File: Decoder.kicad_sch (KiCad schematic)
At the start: 4 parts, among them U1 74LS04, U12 74LS00, U14 74LS138, U7 74LS32

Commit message: Schematic in progress
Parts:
- removed U14: 74LS138, DIP-16__300, symbol 74xx:74LS138
- added U58: 74LS688, symbol 74xx:74LS688
- added U59: 74LS138, Package_DIP:DIP-16_W7.62mm_Socket_LongPads, symbol 74xx:74LS138
- U1, U7: footprint DIP-14__300 -> Package_DIP:DIP-14_W7.62mm_Socket_LongPads
- U21: renamed from U12; footprint DIP-14__300 -> Package_DIP:DIP-14_W7.62mm_Socket_LongPads
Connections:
- net /VMA: now also U58.1 (G)
- net GND: now also U58.10 (GND), U59.16 (VCC)
- net SHADOW-IO: now also U58.2 (P0)
- net VCC: now also U58.12 (R4), U58.14 (R5), U58.16 (R6), U58.17 (P7), U58.18 (R7), U58.20 (VCC), U58.3 (R0), U58.4 (P1), U58.5 (R1), U58.7 (R2), U58.9 (R3), U59.6 (E3), U59.8 (GND)
- net mA10: now also U58.8 (P3)
- net mA11: now also U58.6 (P2)
- net mA8: now also U58.13 (P5)
- net mA9: now also U58.11 (P4)
- new net: U58.19 (P=R), U59.4 (E1), U59.5 (E2)
- new net mA4: U59.1 (A0)
- new net mA5: U59.2 (A1)
- new net mA6: U59.3 (A2)
- new net mA7: U58.15 (P6)
- new net /IOSEL-0EF80: U59.15 (O0)
- new net /IOSEL-0EF90: U59.14 (O1)
- new net /IOSEL-0EFA0: U59.13 (O2)
- new net /IOSEL-0EFB0: U59.12 (O3)
- new net /IOSEL-0EFC0: U59.11 (O4)
- new net /IOSEL-0EFD0: U59.10 (O5)
- new net /IOSEL-0EFE0: U59.9 (O6)
- new net /IOSEL-0EFF0: U59.7 (O7)
- no-connect marks 2 -> 0
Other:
- note added: "$E800 - $E8FF available $E900 - $E9FF available $EA00 - $EAFF MMU CONTROL (20?) $EB00 - $EBFF Video (3) $EC00 - $ECFF VIA0 (16) $ED00 - $EDFF VIA1 (16) $EE00 - $EEFF RTC (16) $EF00 - $EFFF ACIA (4)"
- note removed: "$E800 - $E8FF PTM $E900 - $E9FF available $EA00 - $EAFF MMU CONTROL $EB00 - $EBFF available $EC00 - $ECFF VIA0 $ED00 - $EDFF VIA1 $EE00 - $EEFF PIA $EF00 - $EFFF ACIA"
- note removed: "ON BOARD DEVICE ADDRESS RANGES (256 EACH BLOCK)"
- company: N8VEM Users Group -> (none)
- title: 6809 and 6502 ATX and 6U -> 6809PC

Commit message: PCB in progress
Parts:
- U1, U21, U7: footprint Package_DIP:DIP-14_W7.62mm_Socket_LongPads -> Custom:STD_DDW_DIP14
- U23: renamed from U58; footprint (none) -> Custom:STD_DDW_DIP20
- U24: renamed from U59; footprint Package_DIP:DIP-16_W7.62mm_Socket_LongPads -> Custom:STD_DDW_DIP16
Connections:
- no-connect marks 0 -> 1
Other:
- note added: "$EFF0 - $EFFF available $EFE0 - $EFEF MMU Registers (3) $EFD0 - $EFDF MMU Task Map (16) $EFC0 - $EFCF Video (3) $EFB0 - $EFBF VIA0 (16) $EFA0 - $EFAF VIA1 (16) $EF90 - $EF9F RTC (16) $EF80 - $EF8F ACIA (4)"
- note removed: "$E800 - $E8FF available $E900 - $E9FF available $EA00 - $EAFF MMU CONTROL (20?) $EB00 - $EBFF Video (3) $EC00 - $ECFF VIA0 (16) $ED00 - $EDFF VIA1 (16) $EE00 - $EEFF RTC (16) $EF00 - $EFFF ACIA (4)"
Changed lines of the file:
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@@
 		(color 0 0 0 0)
+	)
+	(no_connect
+		(at 157.48 143.51)
 	)
 	(polyline
@@
 		)
 	)
-	(text "$E800 - $E8FF      available\n$E900 - $E9FF      available\n$EA00 - $EAFF      MMU CONTROL (20?)\n$EB00 - $EBFF      Video (3)\n$EC00 - $ECFF      VIA0 (16)\n$ED00 - $EDFF      VIA1 (16)\n$EE00 - $EEFF      RTC  (16)\n$EF00 - $EFFF      ACIA (4)"
+	(text "$EFF0 - $EFFF      available\n$EFE0 - $EFEF      MMU Registers (3)\n$EFD0 - $EFDF      MMU Task Map (16)\n$EFC0 - $EFCF      Video (3)\n$EFB0 - $EFBF      VIA0 (16)\n$EFA0 - $EFAF      VIA1 (16)\n$EF90 - $EF9F      RTC  (16)\n$EF80 - $EF8F      ACIA (4)"
 		(exclude_from_sim no)
 		(at 206.502 164.338 0)
@@
 			)
 		)
-		(property "Footprint" "Package_DIP:DIP-14_W7.62mm_Socket_LongPads"
+		(property "Footprint" "Custom:STD_DDW_DIP14"
 			(at 168.91 57.15 0)
 			(effects
@@
 			)
 		)
-		(property "Footprint" "Package_DIP:DIP-14_W7.62mm_Socket_LongPads"
+		(property "Footprint" "Custom:STD_DDW_DIP14"
 			(at 121.92 63.5 0)
 			(effects
@@
 			)
 		)
-		(property "Footprint" "Package_DIP:DIP-14_W7.62mm_Socket_LongPads"
+		(property "Footprint" "Custom:STD_DDW_DIP14"
 			(at 220.98 59.69 0)
 			(effects
@@
 		(on_board yes)
 		(dnp no)
-		(property "Reference" "#PWR0204"
+		(property "Reference" "#PWR087"
 			(at 144.78 168.91 0)
 			(effects
@@
 			(project "6809PC-6U"
 				(path "/d94f9d60-5ece-4752-b49c-b0d1c95f35bc/00000000-0000-0000-0000-0000526d3cca"
-					(reference "#PWR0204")
+					(reference "#PWR087")
 					(unit 1)
 				)
@@
 		(on_board yes)
 		(dnp no)
-		(property "Reference" "#PWR0203"
+		(property "Reference" "#PWR086"
 			(at 144.78 133.35 0)
 			(effects
@@
 			(project "6809PC-6U"
 				(path "/d94f9d60-5ece-4752-b49c-b0d1c95f35bc/00000000-0000-0000-0000-0000526d3cca"
-					(reference "#PWR0203")
+					(reference "#PWR086")
 					(unit 1)
 				)
@@
 		(dnp no)
 		(fields_autoplaced yes)
-		(property "Reference" "U58"
+		(property "Reference" "U23"
 			(at 118.11 138.4614 0)
 			(effects
@@
 			)
 		)
-		(property "Footprint" ""
+		(property "Footprint" "Custom:STD_DDW_DIP20"
 			(at 105.41 167.64 0)
 			(effects
@@
 			(project ""
 				(path "/d94f9d60-5ece-4752-b49c-b0d1c95f35bc/00000000-0000-0000-0000-0000526d3cca"
-					(reference "U58")
+					(reference "U23")
 					(unit 1)
 				)
@@
 		(on_board yes)
 		(dnp no)
-		(property "Reference" "U59"
+		(property "Reference" "U24"
 			(at 147.32 166.37 0)
 			(effects
@@
 			)
 		)
-		(property "Footprint" "Package_DIP:DIP-16_W7.62mm_Socket_LongPads"
+		(property "Footprint" "Custom:STD_DDW_DIP16"
 			(at 144.78 153.67 0)
 			(effects
@@
 			(project "6809PC-6U"
 				(path "/d94f9d60-5ece-4752-b49c-b0d1c95f35bc/00000000-0000-0000-0000-0000526d3cca"
-					(reference "U59")
+					(reference "U24")
 					(unit 1)
 				)
@@
 		(on_board yes)
 		(dnp no)
-		(property "Reference" "#PWR0202"
+		(property "Reference" "#PWR085"
 			(at 105.41 199.39 0)
 			(effects
@@
 			(project "6809PC-6U"
 				(path "/d94f9d60-5ece-4752-b49c-b0d1c95f35bc/00000000-0000-0000-0000-0000526d3cca"
-					(reference "#PWR0202")
+					(reference "#PWR085")
 					(unit 1)
 				)
@@
 		(on_board yes)
 		(dnp no)
-		(property "Reference" "#PWR0201"
+		(property "Reference" "#PWR084"
 			(at 105.41 134.62 0)
 			(effects
@@
 			(project "6809PC-6U"
 				(path "/d94f9d60-5ece-4752-b49c-b0d1c95f35bc/00000000-0000-0000-0000-0000526d3cca"
-					(reference "#PWR0201")
+					(reference "#PWR084")
 					(unit 1)
 				)

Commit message: V1.1
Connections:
- net GND: now also U24.8 (GND); no longer U24.16 (VCC)
- net VCC: now also U24.16 (VCC); no longer U24.8 (GND)
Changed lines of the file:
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@@
+	)
+	(junction
+		(at 144.78 168.91)
+		(diameter 0)
+		(color 0 0 0 0)
 	)
 	(junction
@@
 	)
 	(junction
-		(at 144.78 135.89)
-		(diameter 0)
-		(color 0 0 0 0)
-	)
-	(junction
 		(at 92.71 172.72)
 		(diameter 0)
@@
 	(wire
 		(pts
-			(xy 128.27 148.59) (xy 128.27 135.89)
+			(xy 144.78 168.91) (xy 158.75 168.91)
+		)
+		(stroke
+			(width 0)
+			(type default)
+		)
+	)
+	(wire
+		(pts
+			(xy 119.38 168.91) (xy 144.78 168.91)
 		)
 		(stroke
@@
 	(wire
 		(pts
+			(xy 119.38 148.59) (xy 119.38 168.91)
+		)
+		(stroke
+			(width 0)
+			(type default)
+		)
+	)
+	(wire
+		(pts
 			(xy 129.54 63.5) (xy 151.13 63.5)
 		)
@@
 	(wire
 		(pts
-			(xy 128.27 135.89) (xy 144.78 135.89)
-		)
-		(stroke
-			(width 0)
-			(type default)
-		)
-	)
-	(wire
-		(pts
 			(xy 68.58 162.56) (xy 92.71 162.56)
 		)
@@
 	(wire
 		(pts
-			(xy 132.08 148.59) (xy 128.27 148.59)
+			(xy 119.38 148.59) (xy 132.08 148.59)
 		)
 		(stroke
@@
 		(pts
 			(xy 106.68 63.5) (xy 114.3 63.5)
+		)
+		(stroke
+			(width 0)
+			(type default)
+		)
+	)
+	(wire
+		(pts
+			(xy 133.35 135.89) (xy 144.78 135.89)
 		)
 		(stroke
@@
 	(symbol
 		(lib_id "power:GND")
-		(at 144.78 168.91 0)
+		(at 133.35 135.89 0)
 		(unit 1)
 		(exclude_from_sim no)
@@
 		(dnp no)
 		(property "Reference" "#PWR087"
-			(at 144.78 168.91 0)
+			(at 133.35 135.89 0)
 			(effects
 				(font
@@
 		)
 		(property "Value" "GND"
-			(at 144.78 170.688 0)
+			(at 133.35 137.668 0)
 			(effects
 				(font
@@
 		)
 		(property "Footprint" ""
-			(at 144.78 168.91 0)
+			(at 133.35 135.89 0)
 			(effects
 				(font
@@
 		)
 		(property "Datasheet" ""
-			(at 144.78 168.91 0)
+			(at 133.35 135.89 0)
 			(effects
 				(font
@@
 		)
 		(property "Description" "Power symbol creates a global label with name \"GND\" , ground"
-			(at 144.78 168.91 0)
+			(at 133.35 135.89 0)
 			(effects
 				(font
@@
 	(symbol
 		(lib_id "power:VCC")
-		(at 144.78 135.89 0)
+		(at 158.75 168.91 0)
 		(unit 1)
 		(exclude_from_sim no)
@@
 		(dnp no)
 		(property "Reference" "#PWR086"
-			(at 144.78 133.35 0)
+			(at 158.75 166.37 0)
 			(effects
 				(font
@@
 		)
 		(property "Value" "VCC"
-			(at 144.78 132.842 0)
+			(at 158.75 165.862 0)
 			(effects
 				(font
@@
 		)
 		(property "Footprint" ""
-			(at 144.78 135.89 0)
+			(at 158.75 168.91 0)
 			(effects
 				(font
@@
 		)
 		(property "Datasheet" ""
-			(at 144.78 135.89 0)
+			(at 158.75 168.91 0)
 			(effects
 				(font
@@
 		)
 		(property "Description" "Power symbol creates a global label with name \"VCC\""
-			(at 144.78 135.89 0)
-			(effects
-				(font
+			(at 158.75 168.91 0)
+			(effects
+				(font

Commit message: 6809PC work
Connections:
- no-connect marks 1 -> 4
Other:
- note added: "$EFF0 - $EFFF available $EFE0 - $EFEF MMU Registers (3) $EFD0 - $EFDF MMU Task Map (16) $EFC0 - $EFCF available $EFB0 - $EFBF available $EFA0 - $EFAF available $EF90 - $EF9F RTC (16) $EF80 - $EF8F ACIA (4)"
- note removed: "$EFF0 - $EFFF available $EFE0 - $EFEF MMU Registers (3) $EFD0 - $EFDF MMU Task Map (16) $EFC0 - $EFCF Video (3) $EFB0 - $EFBF VIA0 (16) $EFA0 - $EFAF VIA1 (16) $EF90 - $EF9F RTC (16) $EF80 - $EF8F ACIA (4)"
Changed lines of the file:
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@@
 	(title_block
 		(title "6809PC")
-		(date "2025-01-21")
-		(rev "001")
+		(date "2025-05-17")
+		(rev "002")
 		(comment 1 "https://github.com/danwerner21/6809PC")
 		(comment 2 "Based on work by Andrew Lynch and John Coffman")
@@
 	)
 	(no_connect
+		(at 157.48 151.13)
+	)
+	(no_connect
 		(at 157.48 143.51)
+	)
+	(no_connect
+		(at 157.48 156.21)
+	)
+	(no_connect
+		(at 157.48 153.67)
 	)
 	(polyline
@@
 		)
 	)
-	(text "$EFF0 - $EFFF      available\n$EFE0 - $EFEF      MMU Registers (3)\n$EFD0 - $EFDF      MMU Task Map (16)\n$EFC0 - $EFCF      Video (3)\n$EFB0 - $EFBF      VIA0 (16)\n$EFA0 - $EFAF      VIA1 (16)\n$EF90 - $EF9F      RTC  (16)\n$EF80 - $EF8F      ACIA (4)"
+	(text "$EFF0 - $EFFF      available\n$EFE0 - $EFEF      MMU Registers (3)\n$EFD0 - $EFDF      MMU Task Map (16)\n$EFC0 - $EFCF      available\n$EFB0 - $EFBF      available\n$EFA0 - $EFAF      available\n$EF90 - $EF9F      RTC  (16)\n$EF80 - $EF8F      ACIA (4)"
 		(exclude_from_sim no)
 		(at 206.502 164.338 0)

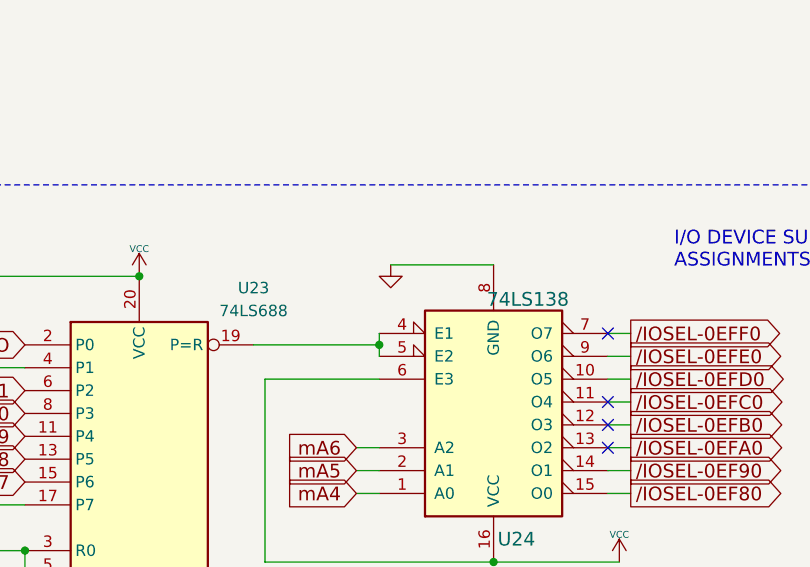
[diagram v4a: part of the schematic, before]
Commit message: fix bus issue
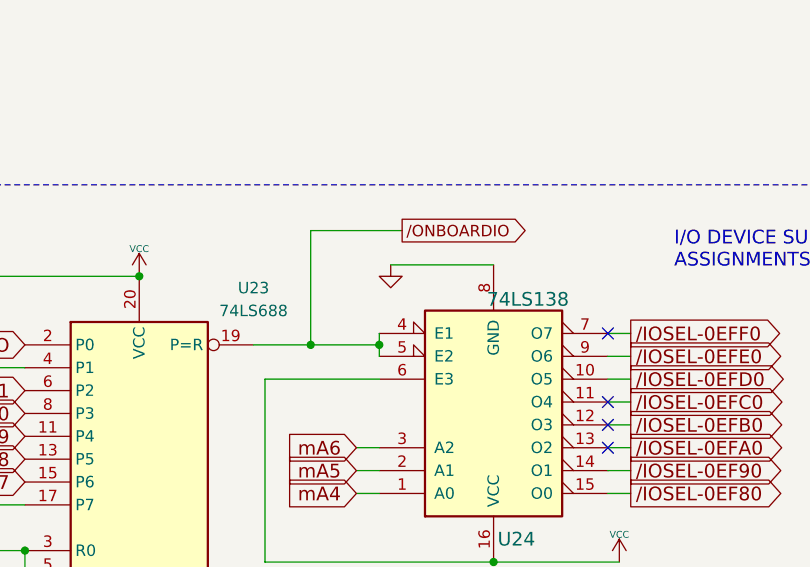
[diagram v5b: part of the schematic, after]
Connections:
- net /ONBOARDIO: now reaches U23.19 (P=R), U24.4 (E1), U24.5 (E2)
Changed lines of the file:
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@@
 	(title_block
 		(title "6809PC")
-		(date "2025-05-17")
-		(rev "002")
+		(date "2025-05-31")
+		(rev "003")
 		(comment 1 "https://github.com/danwerner21/6809PC")
 		(comment 2 "Based on work by Andrew Lynch and John Coffman")
@@
 	)
 	(junction
+		(at 124.46 144.78)
+		(diameter 0)
+		(color 0 0 0 0)
+	)
+	(junction
 		(at 92.71 175.26)
 		(diameter 0)
@@
 	(wire
 		(pts
-			(xy 118.11 144.78) (xy 132.08 144.78)
+			(xy 118.11 144.78) (xy 124.46 144.78)
 		)
 		(stroke
@@
 	(wire
 		(pts
+			(xy 124.46 144.78) (xy 124.46 132.08)
+		)
+		(stroke
+			(width 0)
+			(type default)
+		)
+	)
+	(wire
+		(pts
 			(xy 77.47 190.5) (xy 92.71 190.5)
 		)
@@
 	(wire
 		(pts
+			(xy 124.46 132.08) (xy 134.62 132.08)
+		)
+		(stroke
+			(width 0)
+			(type default)
+		)
+	)
+	(wire
+		(pts
 			(xy 157.48 153.67) (xy 160.02 153.67)
 		)
@@
 		(pts
 			(xy 119.38 148.59) (xy 132.08 148.59)
+		)
+		(stroke
+			(width 0)
+			(type default)
+		)
+	)
+	(wire
+		(pts
+			(xy 124.46 144.78) (xy 132.08 144.78)
 		)
 		(stroke
@@
 				(hide yes)
 			)
+		)
+	)
+	(global_label "{slash}ONBOARDIO"
+		(shape output)
+		(at 134.62 132.08 0)
+		(fields_autoplaced yes)
+		(effects
+			(font
+				(size 1.27 1.27)
+			)
+			(justify left)
+		)
+		(property "Intersheetrefs" "${INTERSHEET_REFS}"
+			(at 149.1069 132.08 0)
+			(effects
+				(font
+					(size 1.27 1.27)
+				)
+				(justify left)
+				(hide yes)
+			)
